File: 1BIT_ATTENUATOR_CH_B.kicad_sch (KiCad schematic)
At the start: 9 parts, among them IC39 ${DEVICE}, IC40 ${DEVICE}, IC41 ${DEVICE}

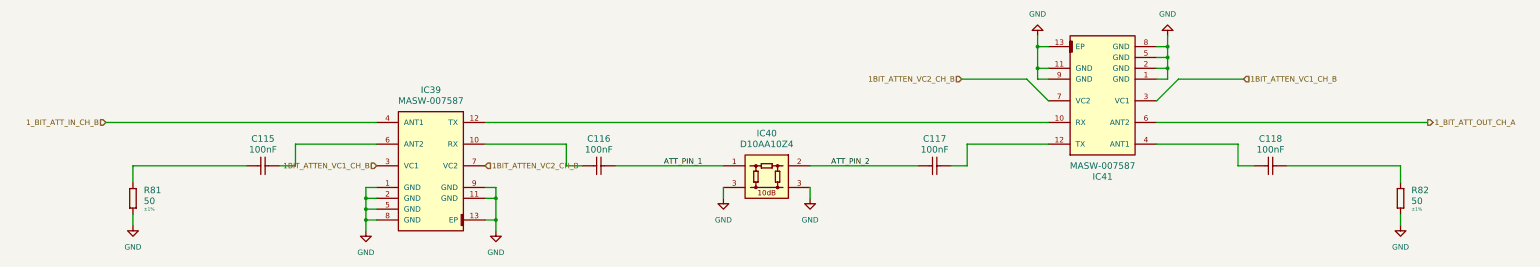
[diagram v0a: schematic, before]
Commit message: Rerouted PCB Logic part
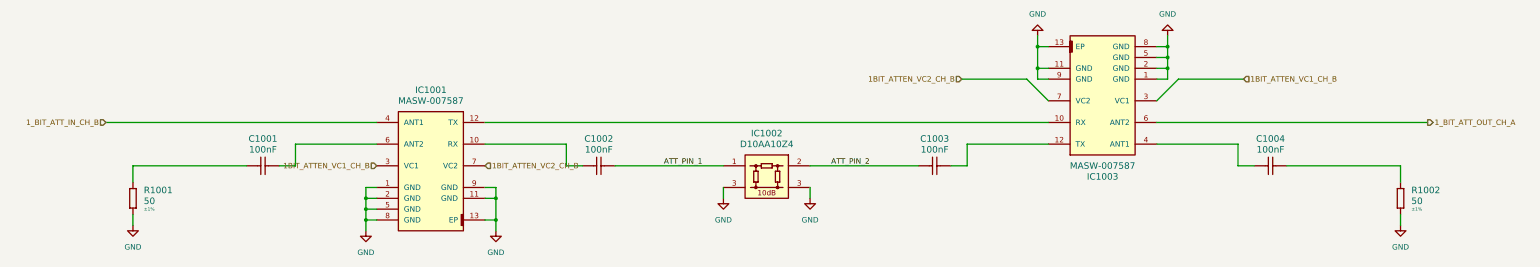
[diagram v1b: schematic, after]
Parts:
- renumbered C115 to C1001, C116 to C1002, C117 to C1003, C118 to C1004, IC39 to IC1001, IC40 to IC1002, IC41 to IC1003, R81 to R1001, R82 to R1002
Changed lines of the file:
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@@
 		(dnp no)
 		(fields_autoplaced yes)
-		(property "Reference" "#PWR0213"
+		(property "Reference" "#PWR01005"
 			(at 217.17 123.19 0)
 			(effects
@@
 			(project "8CH_Analog_Front_END"
 				(path "/41597329-5145-432a-9041-5bc2cec82d9b/e0337a1b-c397-4f99-b607-786eab07764a/92ce1901-304a-4ffa-a31d-87269f893276"
-					(reference "#PWR0213")
+					(reference "#PWR01005")
 					(unit 1)
 				)
@@
 		(dnp no)
 		(fields_autoplaced yes)
-		(property "Reference" "R82"
+		(property "Reference" "R1002"
 			(at 358.14 114.9349 90)
 			(effects
@@
 			(project "8CH_Analog_Front_END"
 				(path "/41597329-5145-432a-9041-5bc2cec82d9b/e0337a1b-c397-4f99-b607-786eab07764a/92ce1901-304a-4ffa-a31d-87269f893276"
-					(reference "R82")
+					(reference "R1002")
 					(unit 1)
 				)
@@
 		(dnp no)
 		(fields_autoplaced yes)
-		(property "Reference" "#PWR0198"
+		(property "Reference" "#PWR01003"
 			(at 143.51 130.81 0)
 			(effects
@@
 			(project "8CH_Analog_Front_END"
 				(path "/41597329-5145-432a-9041-5bc2cec82d9b/e0337a1b-c397-4f99-b607-786eab07764a/92ce1901-304a-4ffa-a31d-87269f893276"
-					(reference "#PWR0198")
+					(reference "#PWR01003")
 					(unit 1)
 				)
@@
 		(dnp no)
 		(fields_autoplaced yes)
-		(property "Reference" "IC39"
+		(property "Reference" "IC1001"
 			(at 128.27 91.44 0)
 			(effects
@@
 			(project "8CH_Analog_Front_END"
 				(path "/41597329-5145-432a-9041-5bc2cec82d9b/e0337a1b-c397-4f99-b607-786eab07764a/92ce1901-304a-4ffa-a31d-87269f893276"
-					(reference "IC39")
+					(reference "IC1001")
 					(unit 1)
 				)
@@
 		(dnp no)
 		(fields_autoplaced yes)
-		(property "Reference" "C118"
+		(property "Reference" "C1004"
 			(at 325.12 102.87 0)
 			(effects
@@
 			(project "8CH_Analog_Front_END"
 				(path "/41597329-5145-432a-9041-5bc2cec82d9b/e0337a1b-c397-4f99-b607-786eab07764a/92ce1901-304a-4ffa-a31d-87269f893276"
-					(reference "C118")
+					(reference "C1004")
 					(unit 1)
 				)
@@
 		(dnp no)
 		(fields_autoplaced yes)
-		(property "Reference" "R81"
+		(property "Reference" "R1001"
 			(at 60.96 114.9349 90)
 			(effects
@@
 			(project "8CH_Analog_Front_END"
 				(path "/41597329-5145-432a-9041-5bc2cec82d9b/e0337a1b-c397-4f99-b607-786eab07764a/92ce1901-304a-4ffa-a31d-87269f893276"
-					(reference "R81")
+					(reference "R1001")
 					(unit 1)
 				)
@@
 		(dnp no)
 		(fields_autoplaced yes)
-		(property "Reference" "IC41"
+		(property "Reference" "IC1003"
 			(at 285.75 111.76 0)
 			(effects
@@
 			(project "8CH_Analog_Front_END"
 				(path "/41597329-5145-432a-9041-5bc2cec82d9b/e0337a1b-c397-4f99-b607-786eab07764a/92ce1901-304a-4ffa-a31d-87269f893276"
-					(reference "IC41")
+					(reference "IC1003")
 					(unit 1)
 				)
@@
 		(dnp no)
 		(fields_autoplaced yes)
-		(property "Reference" "#PWR0196"
+		(property "Reference" "#PWR01001"
 			(at 58.42 129.54 0)
 			(effects
@@
 			(project "8CH_Analog_Front_END"
 				(path "/41597329-5145-432a-9041-5bc2cec82d9b/e0337a1b-c397-4f99-b607-786eab07764a/92ce1901-304a-4ffa-a31d-87269f893276"
-					(reference "#PWR0196")
+					(reference "#PWR01001")
 					(unit 1)
 				)
@@
 		(dnp no)
 		(fields_autoplaced yes)
-		(property "Reference" "#PWR0200"
+		(property "Reference" "#PWR01004"
 			(at 196.85 123.19 0)
 			(effects
@@
 			(project "8CH_Analog_Front_END"
 				(path "/41597329-5145-432a-9041-5bc2cec82d9b/e0337a1b-c397-4f99-b607-786eab07764a/92ce1901-304a-4ffa-a31d-87269f893276"
-					(reference "#PWR0200")
+					(reference "#PWR01004")
 					(unit 1)
 				)
@@
 		(dnp no)
 		(fields_autoplaced yes)
-		(property "Reference" "C115"
+		(property "Reference" "C1001"
 			(at 88.9 102.87 0)
 			(effects
@@
 			(project "8CH_Analog_Front_END"
 				(path "/41597329-5145-432a-9041-5bc2cec82d9b/e0337a1b-c397-4f99-b607-786eab07764a/92ce1901-304a-4ffa-a31d-87269f893276"
-					(reference "C115")
+					(reference "C1001")
 					(unit 1)
 				)
@@
 		(dnp no)
 		(fields_autoplaced yes)
-		(property "Reference" "#PWR0199"
+		(property "Reference" "#PWR01006"
 			(at 270.51 72.39 0)
 			(effects
@@
 			(project "8CH_Analog_Front_END"
 				(path "/41597329-5145-432a-9041-5bc2cec82d9b/e0337a1b-c397-4f99-b607-786eab07764a/92ce1901-304a-4ffa-a31d-87269f893276"
-					(reference "#PWR0199")
+					(reference "#PWR01006")
 					(unit 1)
 				)
@@
 		(dnp no)
 		(fields_autoplaced yes)
-		(property "Reference" "IC40"
+		(property "Reference" "IC1002"
 			(at 207.01 101.6 0)
 			(effects
@@
 			(project "8CH_Analog_Front_END"
 				(path "/41597329-5145-432a-9041-5bc2cec82d9b/e0337a1b-c397-4f99-b607-786eab07764a/92ce1901-304a-4ffa-a31d-87269f893276"
-					(reference "IC40")
+					(reference "IC1002")
 					(unit 1)
 				)
@@
 		(dnp no)
 		(fields_autoplaced yes)
-		(property "Reference" "#PWR0197"
+		(property "Reference" "#PWR01002"
 			(at 113.03 130.81 0)
 			(effects
@@
 			(project "8CH_Analog_Front_END"
 				(path "/41597329-5145-432a-9041-5bc2cec82d9b/e0337a1b-c397-4f99-b607-786eab07764a/92ce1901-304a-4ffa-a31d-87269f893276"
-					(reference "#PWR0197")
+					(reference "#PWR01002")
 					(unit 1)
 				)
@@
 		(dnp no)
 		(fields_autoplaced yes)
-		(property "Reference" "#PWR0194"
+		(property "Reference" "#PWR01008"
 			(at 355.6 129.54 0)
 			(effects
@@
 			(project "8CH_Analog_Front_END"
 				(path "/41597329-5145-432a-9041-5bc2cec82d9b/e0337a1b-c397-4f99-b607-786eab07764a/92ce1901-304a-4ffa-a31d-87269f893276"
-					(reference "#PWR0194")
+					(reference "#PWR01008")
 					(unit 1)
 				)
@@
 		(dnp no)
 		(fields_autoplaced yes)
-		(property "Reference" "#PWR0195"
+		(property "Reference" "#PWR01007"
 			(at 300.99 72.39 0)
 			(effects
@@
 			(project "8CH_Analog_Front_END"
 				(path "/41597329-5145-432a-9041-5bc2cec82d9b/e0337a1b-c397-4f99-b607-786eab07764a/92ce1901-304a-4ffa-a31d-87269f893276"
-					(reference "#PWR0195")
+					(reference "#PWR01007")
 					(unit 1)
 				)
@@
 		(dnp no)
 		(fields_autoplaced yes)
-		(property "Reference" "C116"
+		(property "Reference" "C1002"
 			(at 167.64 102.87 0)
 			(effects
@@
 			(project "8CH_Analog_Front_END"
 				(path "/41597329-5145-432a-9041-5bc2cec82d9b/e0337a1b-c397-4f99-b607-786eab07764a/92ce1901-304a-4ffa-a31d-87269f893276"
-					(reference "C116")
+					(reference "C1002")
 					(unit 1)
 				)
@@
 		(dnp no)
 		(fields_autoplaced yes)
-		(property "Reference" "C117"
+		(property "Reference" "C1003"
 			(at 246.38 102.87 0)
 			(effects
@@
 			(project "8CH_Analog_Front_END"
 				(path "/41597329-5145-432a-9041-5bc2cec82d9b/e0337a1b-c397-4f99-b607-786eab07764a/92ce1901-304a-4ffa-a31d-87269f893276"
-					(reference "C117")
+					(reference "C1003")
 					(unit 1)
 				)
